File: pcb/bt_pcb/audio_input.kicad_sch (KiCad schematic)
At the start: 33 parts, among them J19 ReanNYS216G, J20 ReanNYS216G, U4 MCP6004

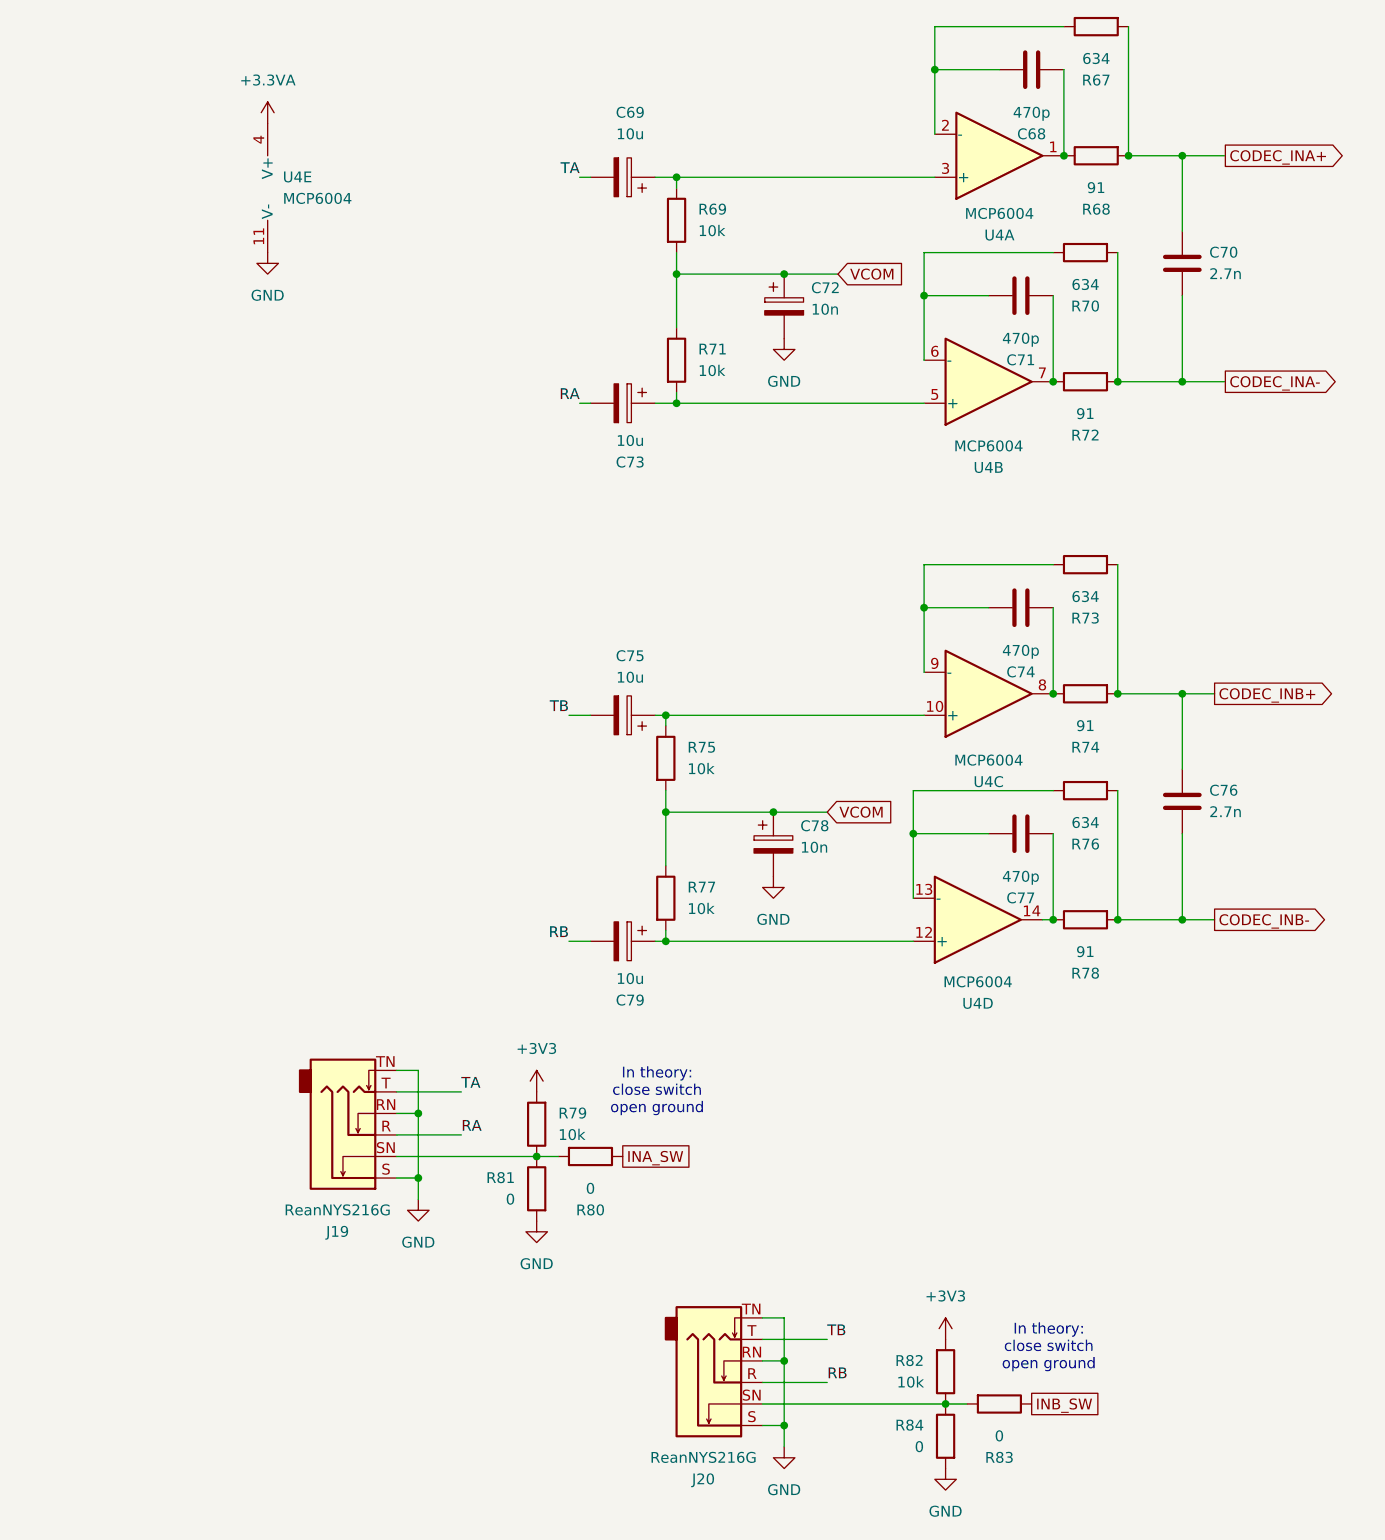
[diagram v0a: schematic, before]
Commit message: doing pcb from scratch again
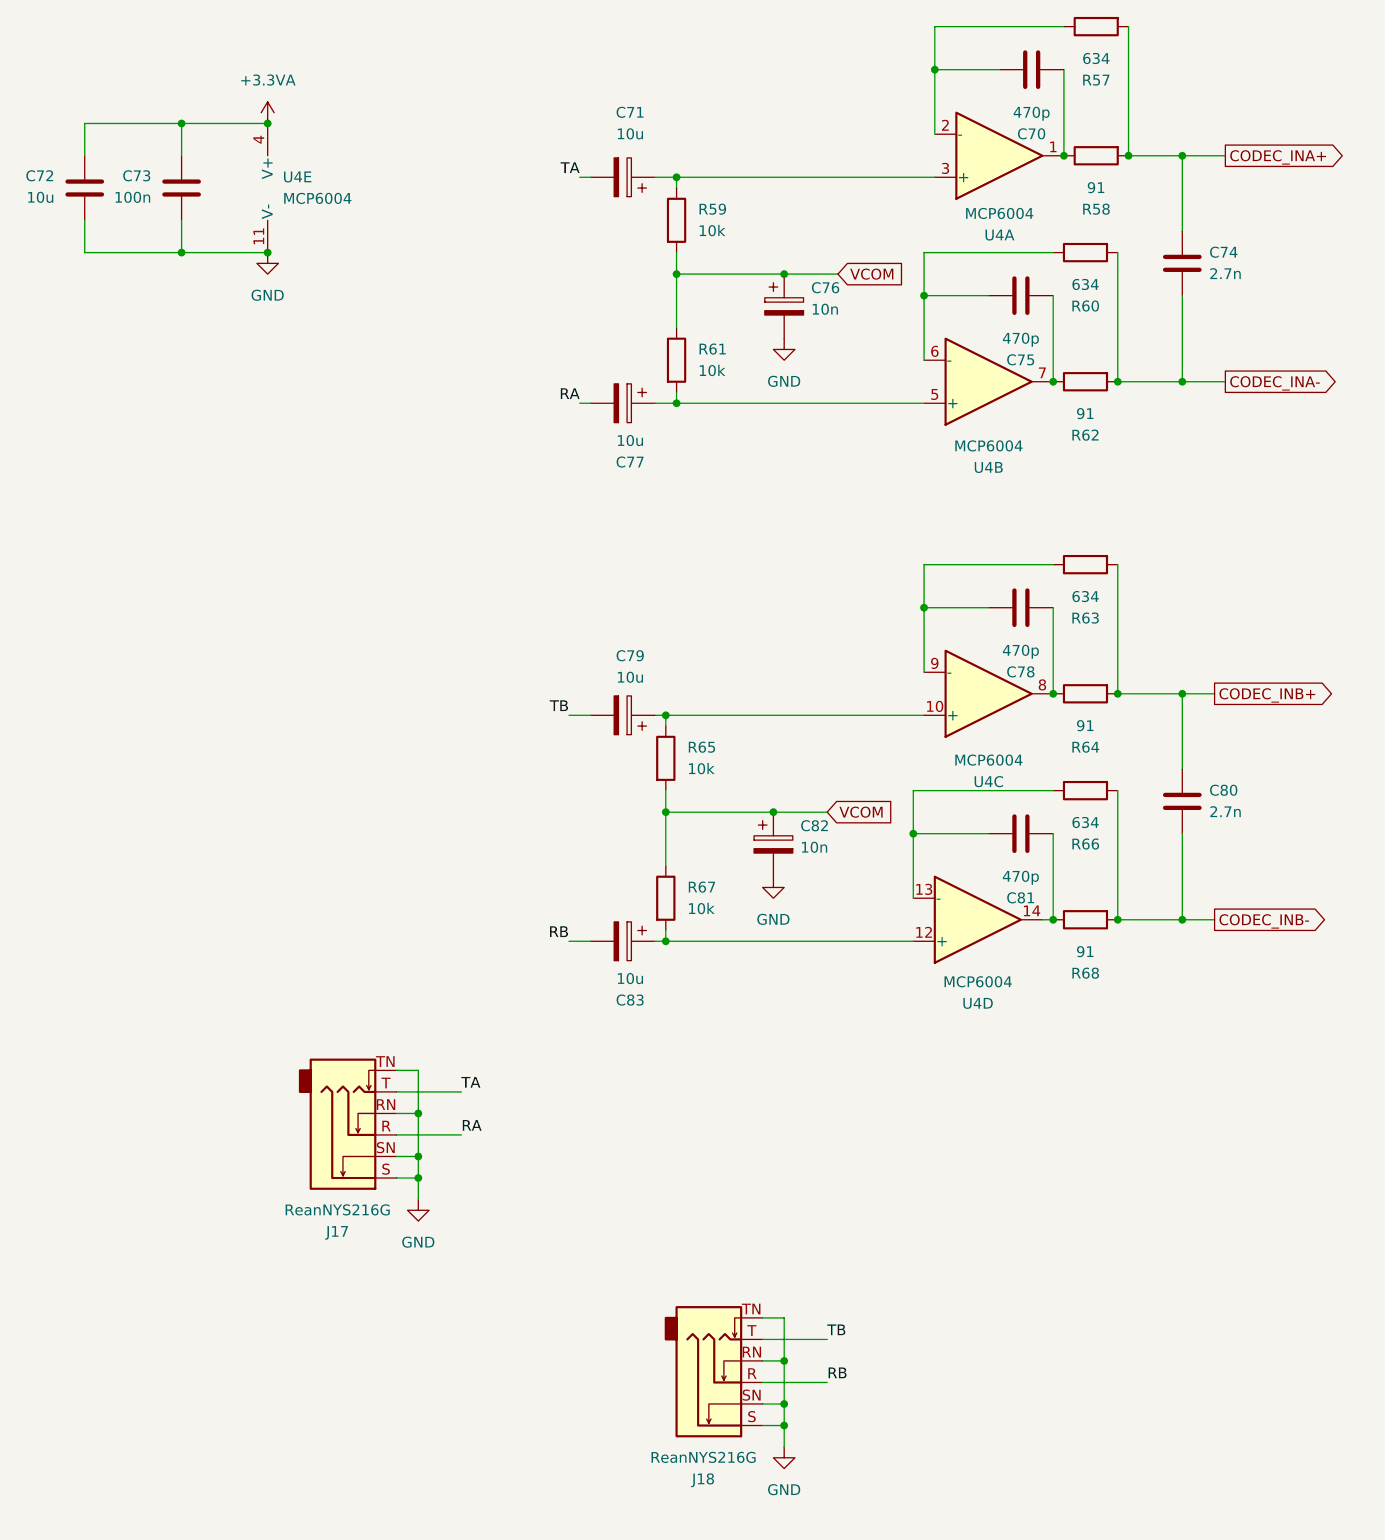
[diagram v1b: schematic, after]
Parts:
- removed R79, R82: 10k, Resistor_SMD:R_0603_1608Metric_Pad0.98x0.95mm_HandSolder, symbol Device:R
- removed R80, R81, R83, R84: 0, Resistor_SMD:R_0603_1608Metric_Pad0.98x0.95mm_HandSolder, symbol Device:R
- added C72: 10u, Capacitor_SMD:C_0603_1608Metric_Pad1.08x0.95mm_HandSolder, symbol Device:C
- added C73: 100n, Capacitor_SMD:C_0603_1608Metric_Pad1.08x0.95mm_HandSolder, symbol Device:C
- renumbered C68 to C70, C69 to C71, C70 to C74, C71 to C75, C72 to C76, C73 to C77, C74 to C78, C75 to C79, C76 to C80, C77 to C81, C78 to C82, C79 to C83, J19 to J17, J20 to J18, R67 to R57, R68 to R58, R69 to R59, R70 to R60, R71 to R61, R72 to R62, R73 to R63, R74 to R64, R75 to R65, R76 to R66, R77 to R67, R78 to R68
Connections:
- net +3.3VA: now also C72.1, C73.1
- net GND: now also J17.SN, J18.SN, C72.2, C73.2
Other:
- note removed: "In theory: close switch open ground"

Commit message: maybe???
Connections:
- net at C77.1, R61.2: now also U4.3 (+); no longer U4.5 (+)
- net at C70.1, R58.1: now also U4.7; no longer U4.1
- net at C70.2, R57.1: now also U4.6 (-); no longer U4.2 (-)
- net at C83.1, R67.2: now also U4.10 (+); no longer U4.12 (+)
- net at C81.2, R66.1: now also U4.9 (-); no longer U4.13 (-)
- net at C81.1, R68.1: now also U4.8; no longer U4.14
- net at C78.1, R64.1: now also U4.14; no longer U4.8
- net at C78.2, R63.1: now also U4.13 (-); no longer U4.9 (-)
- net at C71.1, R59.1: now also U4.5 (+); no longer U4.3 (+)
- net at C75.2, R60.1: now also U4.2 (-); no longer U4.6 (-)
- net at C75.1, R62.1: now also U4.1; no longer U4.7
- net at C79.1, R65.1: now also U4.12 (+); no longer U4.10 (+)

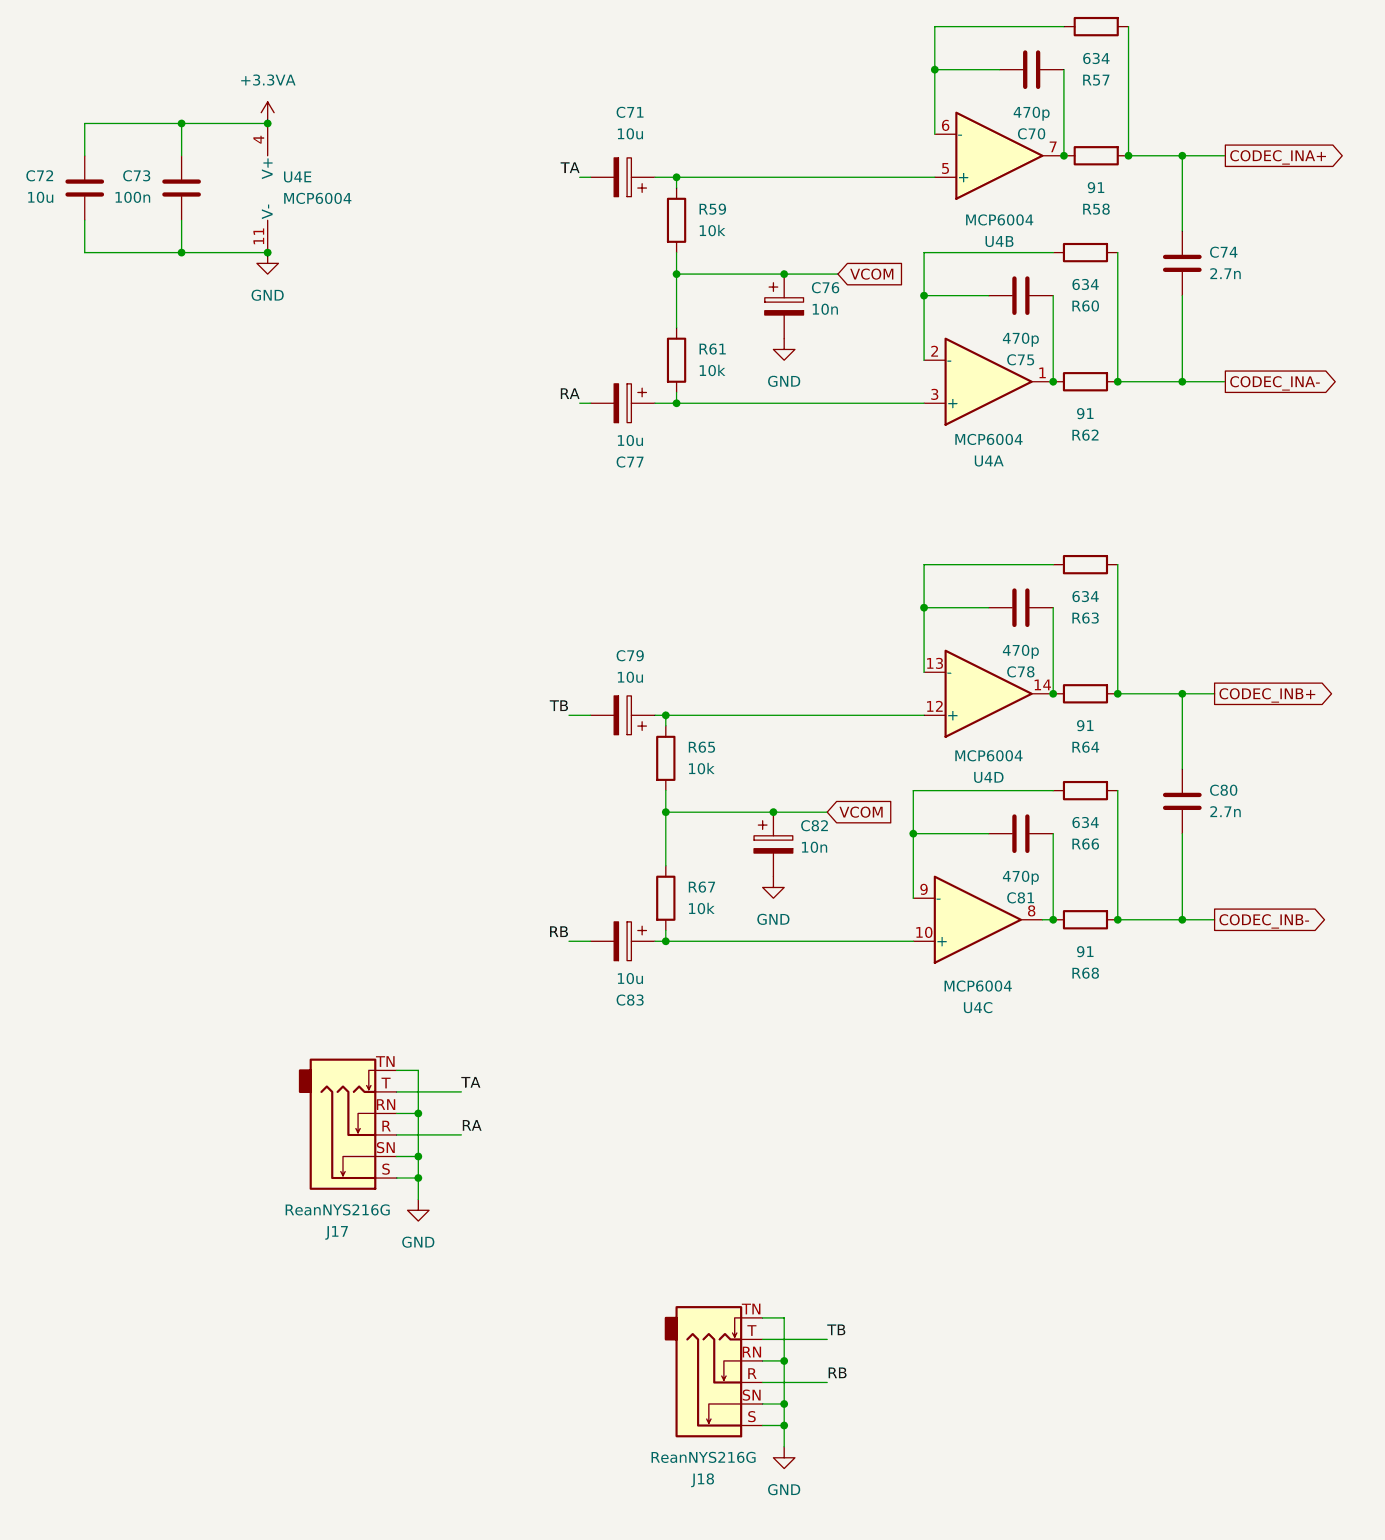
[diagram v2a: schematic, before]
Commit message: redo of power supply
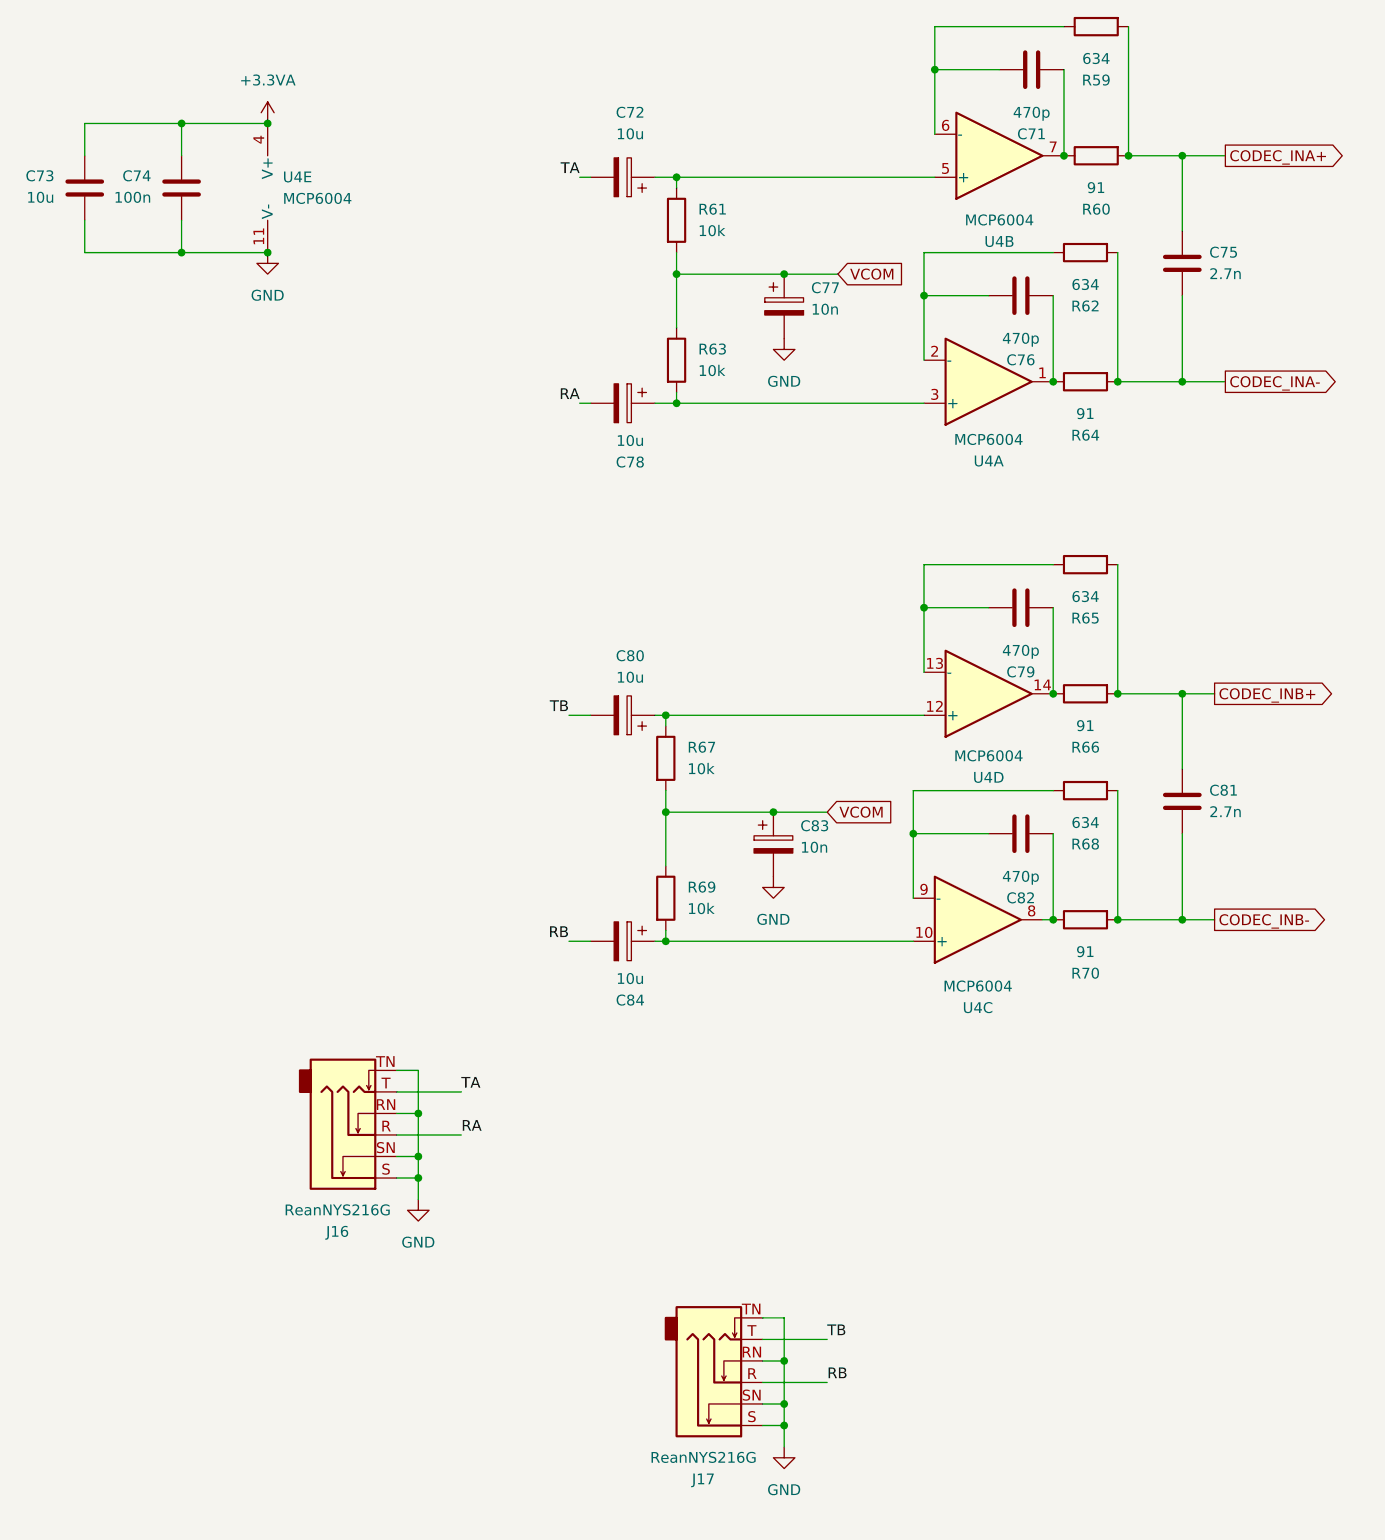
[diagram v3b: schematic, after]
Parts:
- renumbered C70 to C71, C71 to C72, C72 to C73, C73 to C74, C74 to C75, C75 to C76, C76 to C77, C77 to C78, C78 to C79, C79 to C80, C80 to C81, C81 to C82, C82 to C83, C83 to C84, J17 to J16, J18 to J17, R57 to R59, R58 to R60, R59 to R61, R60 to R62, R61 to R63, R62 to R64, R63 to R65, R64 to R66, R65 to R67, R66 to R68, R67 to R69, R68 to R70

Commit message: made a bom
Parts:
- C73: footprint Capacitor_SMD:C_0603_1608Metric_Pad1.08x0.95mm_HandSolder -> Capacitor_SMD:C_0805_2012Metric_Pad1.18x1.45mm_HandSolder
